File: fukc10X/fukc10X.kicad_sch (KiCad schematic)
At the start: 18 parts, among them J1 SM04B-SRSS-TB, U1 XC6206P332MR, U2 STM32F072CBT6

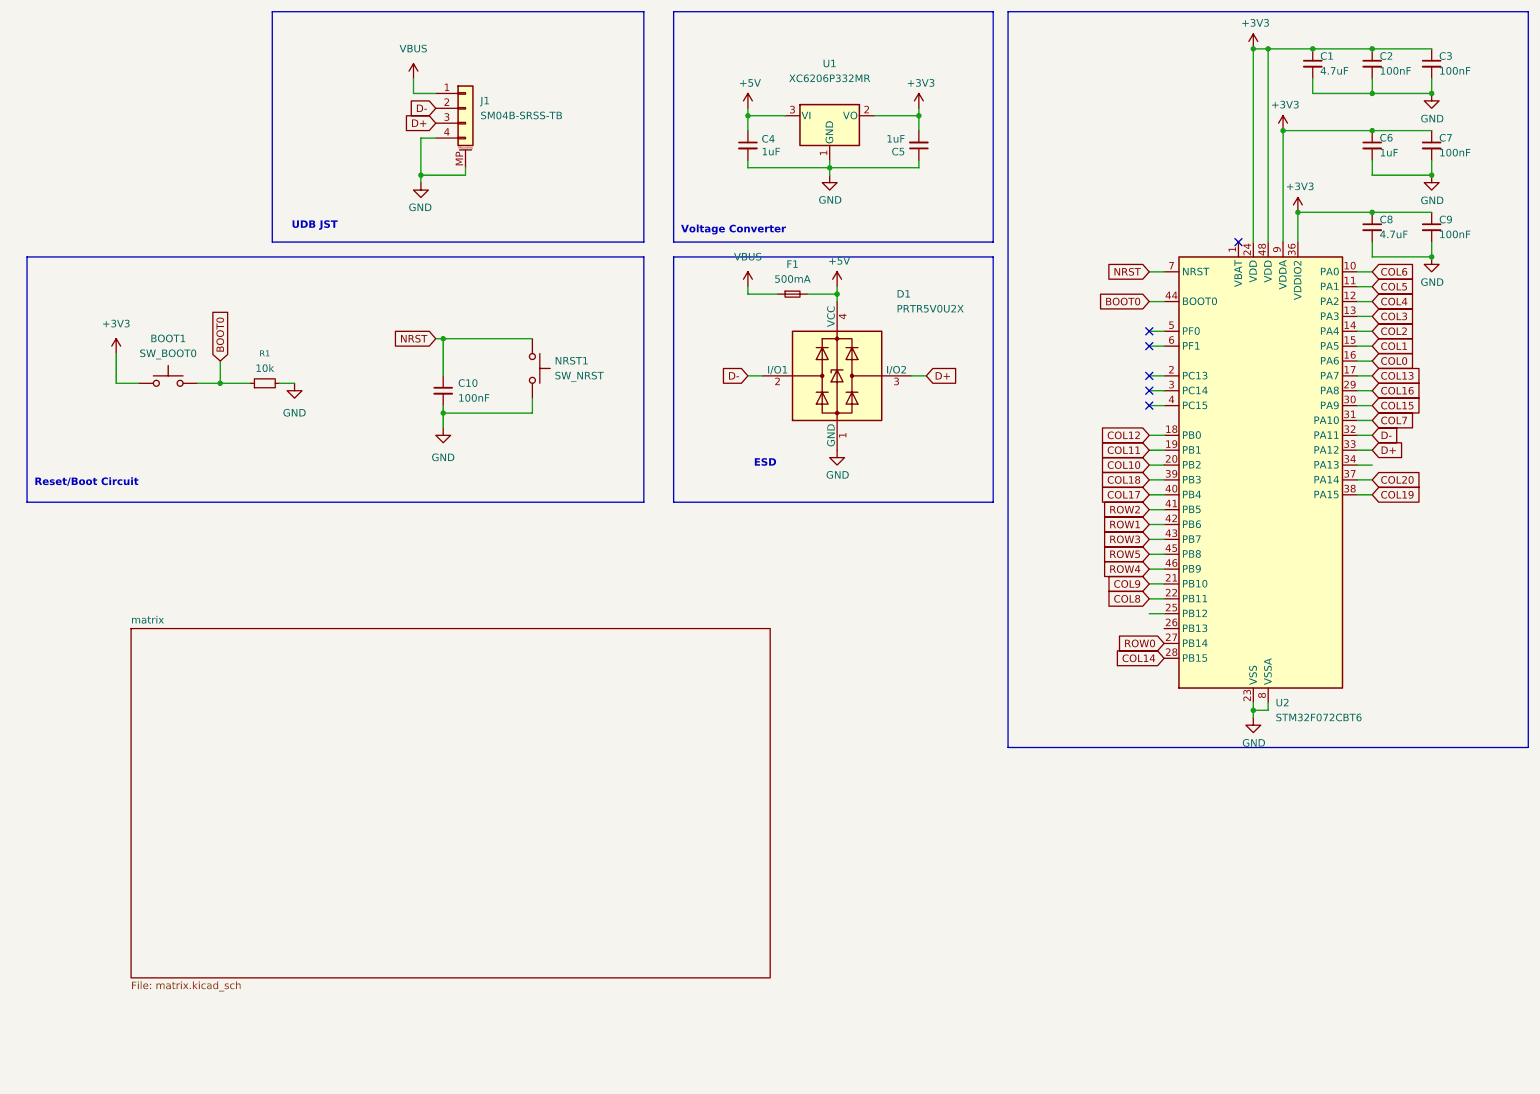
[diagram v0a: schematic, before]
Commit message: Extended Matrix. Added split r-shift and split l-shift. LED support. Removed three of the 4 top right keys because ugly and to make space for indicator leds there
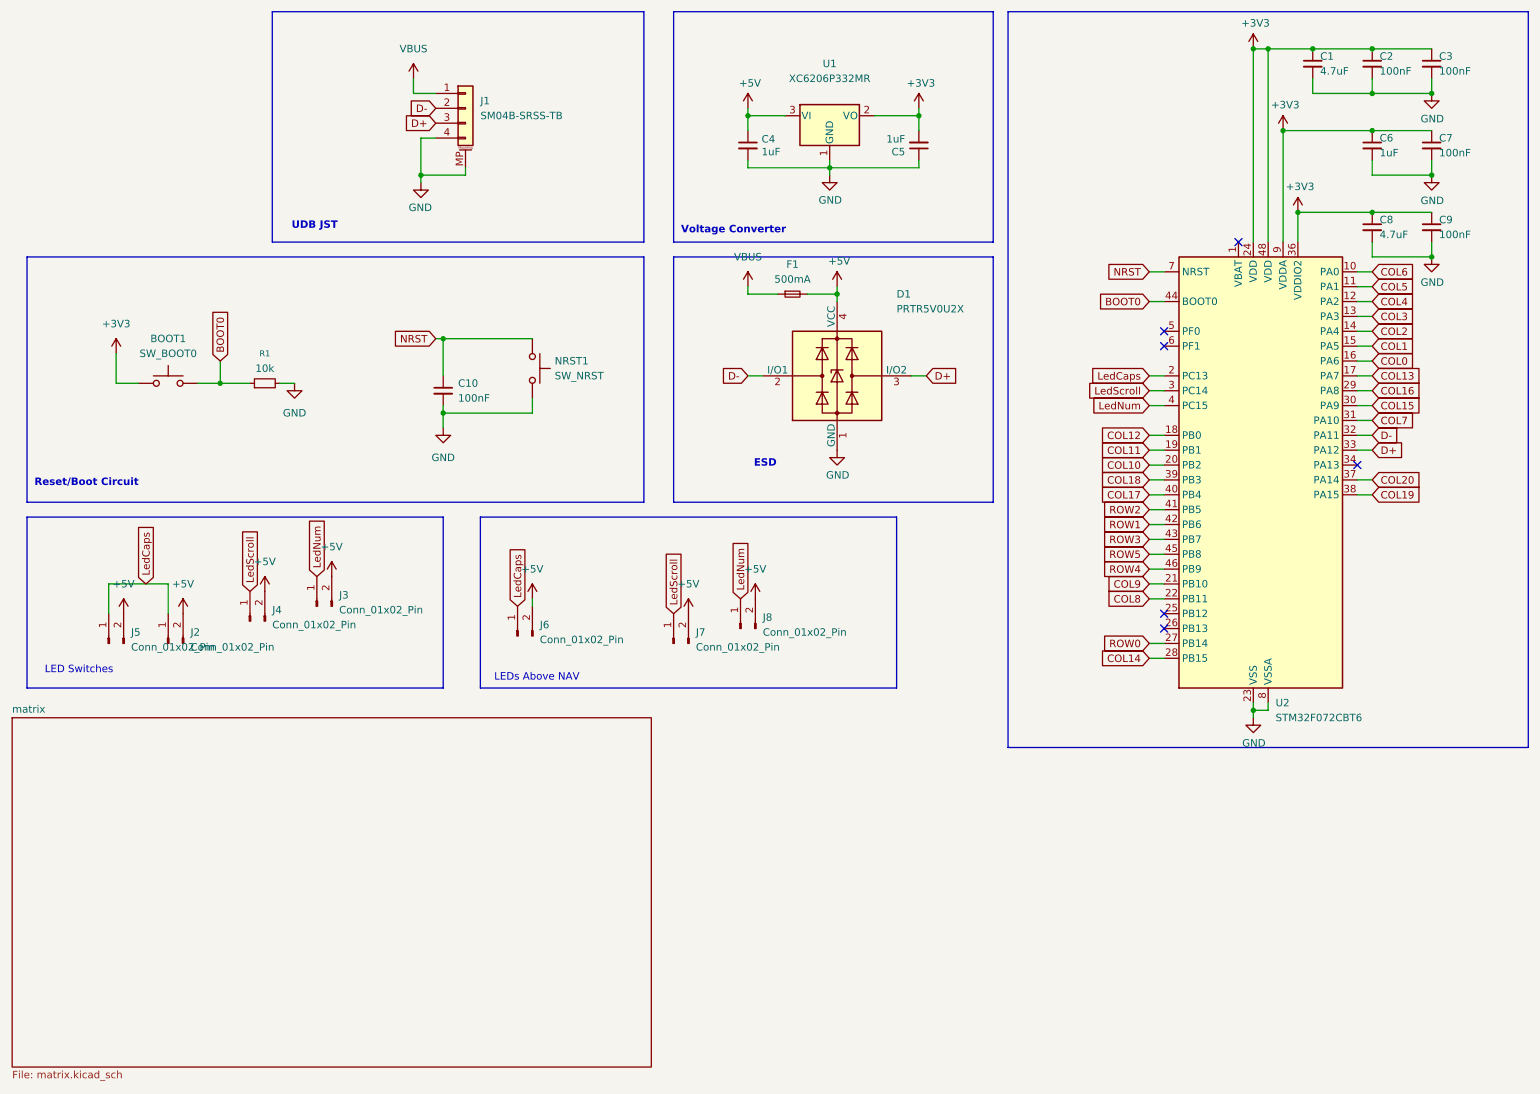
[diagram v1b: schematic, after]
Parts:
- added J2, J3, J4, J6, J7, J8: Conn_01x02_Pin, PCM_marbastlib-mx:LED_MX_3mm, symbol Connector:Conn_01x02_Pin
- added J5: Conn_01x02_Pin, PCM_marbastlib-mx:LED_MX_3mm-ROT, symbol Connector:Conn_01x02_Pin
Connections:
- net +5V: now also J2.2 (Pin_2), J3.2 (Pin_2), J4.2 (Pin_2), J5.2 (Pin_2), J6.2 (Pin_2), J7.2 (Pin_2), J8.2 (Pin_2)
- net LedCaps: now reaches U2.2 (PC13)
- net LedCaps: now also J2.1 (Pin_1), J5.1 (Pin_1), J6.1 (Pin_1)
- net LedScroll: now reaches U2.3 (PC14)
- net LedScroll: now also J4.1 (Pin_1), J7.1 (Pin_1)
- net LedNum: now reaches U2.4 (PC15)
- net LedNum: now also J3.1 (Pin_1), J8.1 (Pin_1)
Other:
- note added: "LED Switches"
- note added: "LEDs Above NAV"

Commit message: Added some Silkscreen Text aswell as spare diodes
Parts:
- added D116, D117, D118, D119, D120, D121, D122, D18, D19, D20, D63, D66: D_Small, Diode_SMD:D_SOD-123, symbol Device:D_Small
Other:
- note added: "Spare Diodes"

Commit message: added split backspace + some updates to the matrix
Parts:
- BOOT1, NRST1: LCSC (none) -> C318884
- C10: LCSC (none) -> C1525
- C2, C3, C7, C9: LCSC C1525 -> C1525
- D116, D117, D118, D119, D120, D121, D122, D18, D19, D20, D63, D66: LCSC (none) -> C81598
- F1: LCSC (none) -> C69688
- R1: LCSC (none) -> C25744
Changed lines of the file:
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@@
 			)
 		)
-		(property "LCSC" "C1525"
+		(property "LCSC" "C1525 "
 			(at 267.97 27.94 0)
 			(hide yes)
@@
 			)
 		)
+		(property "LCSC" "C318884 "
+			(at 50.8 78.74 0)
+			(hide yes)
+			(show_name no)
+			(do_not_autoplace no)
+			(effects
+				(font
+					(size 1.27 1.27)
+				)
+			)
+		)
 		(pin "2"
 		)
@@
 			)
 		)
-		(property "LCSC" "C1525"
+		(property "LCSC" "C1525 "
 			(at 267.97 55.88 0)
 			(hide yes)
@@
 			)
 		)
+		(property "LCSC" "C81598 "
+			(at 168.91 149.86 0)
+			(hide yes)
+			(show_name no)
+			(do_not_autoplace no)
+			(effects
+				(font
+					(size 1.27 1.27)
+				)
+			)
+		)
 		(pin "1"
 		)
@@
 			)
 		)
+		(property "LCSC" "C81598 "
+			(at 181.61 158.75 0)
+			(hide yes)
+			(show_name no)
+			(do_not_autoplace no)
+			(effects
+				(font
+					(size 1.27 1.27)
+				)
+			)
+		)
 		(pin "1"
 		)
@@
 			)
 		)
+		(property "LCSC" "C81598 "
+			(at 168.91 158.75 0)
+			(hide yes)
+			(show_name no)
+			(do_not_autoplace no)
+			(effects
+				(font
+					(size 1.27 1.27)
+				)
+			)
+		)
 		(pin "1"
 		)
@@
 			)
 		)
+		(property "LCSC" "C81598 "
+			(at 176.53 143.51 0)
+			(hide yes)
+			(show_name no)
+			(do_not_autoplace no)
+			(effects
+				(font
+					(size 1.27 1.27)
+				)
+			)
+		)
 		(pin "1"
 		)
@@
 			)
 		)
+		(property "LCSC" "C81598 "
+			(at 162.56 149.86 0)
+			(hide yes)
+			(show_name no)
+			(do_not_autoplace no)
+			(effects
+				(font
+					(size 1.27 1.27)
+				)
+			)
+		)
 		(pin "1"
 		)
@@
 			)
 		)
-		(property "LCSC" "C1525"
+		(property "LCSC" "C1525 "
 			(at 267.97 41.91 0)
 			(hide yes)
@@
 			)
 		)
+		(property "LCSC" "C25744 "
+			(at 67.31 78.74 90)
+			(hide yes)
+			(show_name no)
+			(do_not_autoplace no)
+			(effects
+				(font
+					(size 1.27 1.27)
+				)
+			)
+		)
 		(pin "1"
 		)
@@
 			)
 		)
+		(property "LCSC" "C81598 "
+			(at 181.61 149.86 0)
+			(hide yes)
+			(show_name no)
+			(do_not_autoplace no)
+			(effects
+				(font
+					(size 1.27 1.27)
+				)
+			)
+		)
 		(pin "1"
 		)
@@
 			)
 		)
+		(property "LCSC" "C69688 "
+			(at 157.48 63.5 0)
+			(hide yes)
+			(show_name no)
+			(do_not_autoplace no)
+			(effects
+				(font
+					(size 1.27 1.27)
+				)
+			)
+		)
 		(pin "2"
 		)
@@
 			)
 		)
+		(property "LCSC" "C81598 "
+			(at 162.56 143.51 0)
+			(hide yes)
+			(show_name no)
+			(do_not_autoplace no)
+			(effects
+				(font
+					(size 1.27 1.27)
+				)
+			)
+		)
 		(pin "1"
 		)
@@
 			)
 		)
+		(property "LCSC" "C81598 "
+			(at 161.29 158.75 0)
+			(hide yes)
+			(show_name no)
+			(do_not_autoplace no)
+			(effects
+				(font
+					(size 1.27 1.27)
+				)
+			)
+		)
 		(pin "1"
 		)
@@
 			)
 		)
+		(property "LCSC" "C1525 "
+			(at 97.79 80.01 0)
+			(hide yes)
+			(show_name no)
+			(do_not_autoplace no)
+			(effects
+				(font
+					(size 1.27 1.27)
+				)
+			)
+		)
 		(pin "2"
 		)
@@
 			)
 		)
-		(property "LCSC" "C1525"
+		(property "LCSC" "C1525 "
 			(at 257.81 27.94 0)
 			(hide yes)
@@
 			)
 		)
+		(property "LCSC" "C81598 "
+			(at 170.18 143.51 0)
+			(hide yes)
+			(show_name no)
+			(do_not_autoplace no)
+			(effects
+				(font
+					(size 1.27 1.27)
+				)
+			)
+		)
 		(pin "1"
 		)
@@
 			)
 		)
+		(property "LCSC" "C81598 "
+			(at 175.26 149.86 0)
+			(hide yes)
+			(show_name no)
+			(do_not_autoplace no)
+			(effects
+				(font
+					(size 1.27 1.27)
+				)
+			)
+		)
 		(pin "1"
 		)
@@
 			)
 		)
+		(property "LCSC" "C318884 "
+			(at 113.03 76.2 90)
+			(hide yes)
+			(show_name no)
+			(do_not_autoplace no)
+			(effects
+				(font
+					(size 1.27 1.27)
+				)
+			)
+		)
 		(pin "2"
 		)
@@
 			)
 		)
+		(property "LCSC" "C81598 "
+			(at 182.88 143.51 0)
+			(hide yes)
+			(show_name no)
+			(do_not_autoplace no)
+			(effects
+				(font
+					(size 1.27 1.27)
+				)
+			)
+		)
 		(pin "1"
 		)
@@
 			(at 175.26 158.75 0)
 			(hide yes)
+			(show_name no)
+			(do_not_autoplace no)
+			(effects
+				(font
+					(size 1.27 1.27)
+				)
+			)
+		)
+		(property "LCSC" "C81598 "
+			(at 175.26 158.75 0)
+			(hide yes)

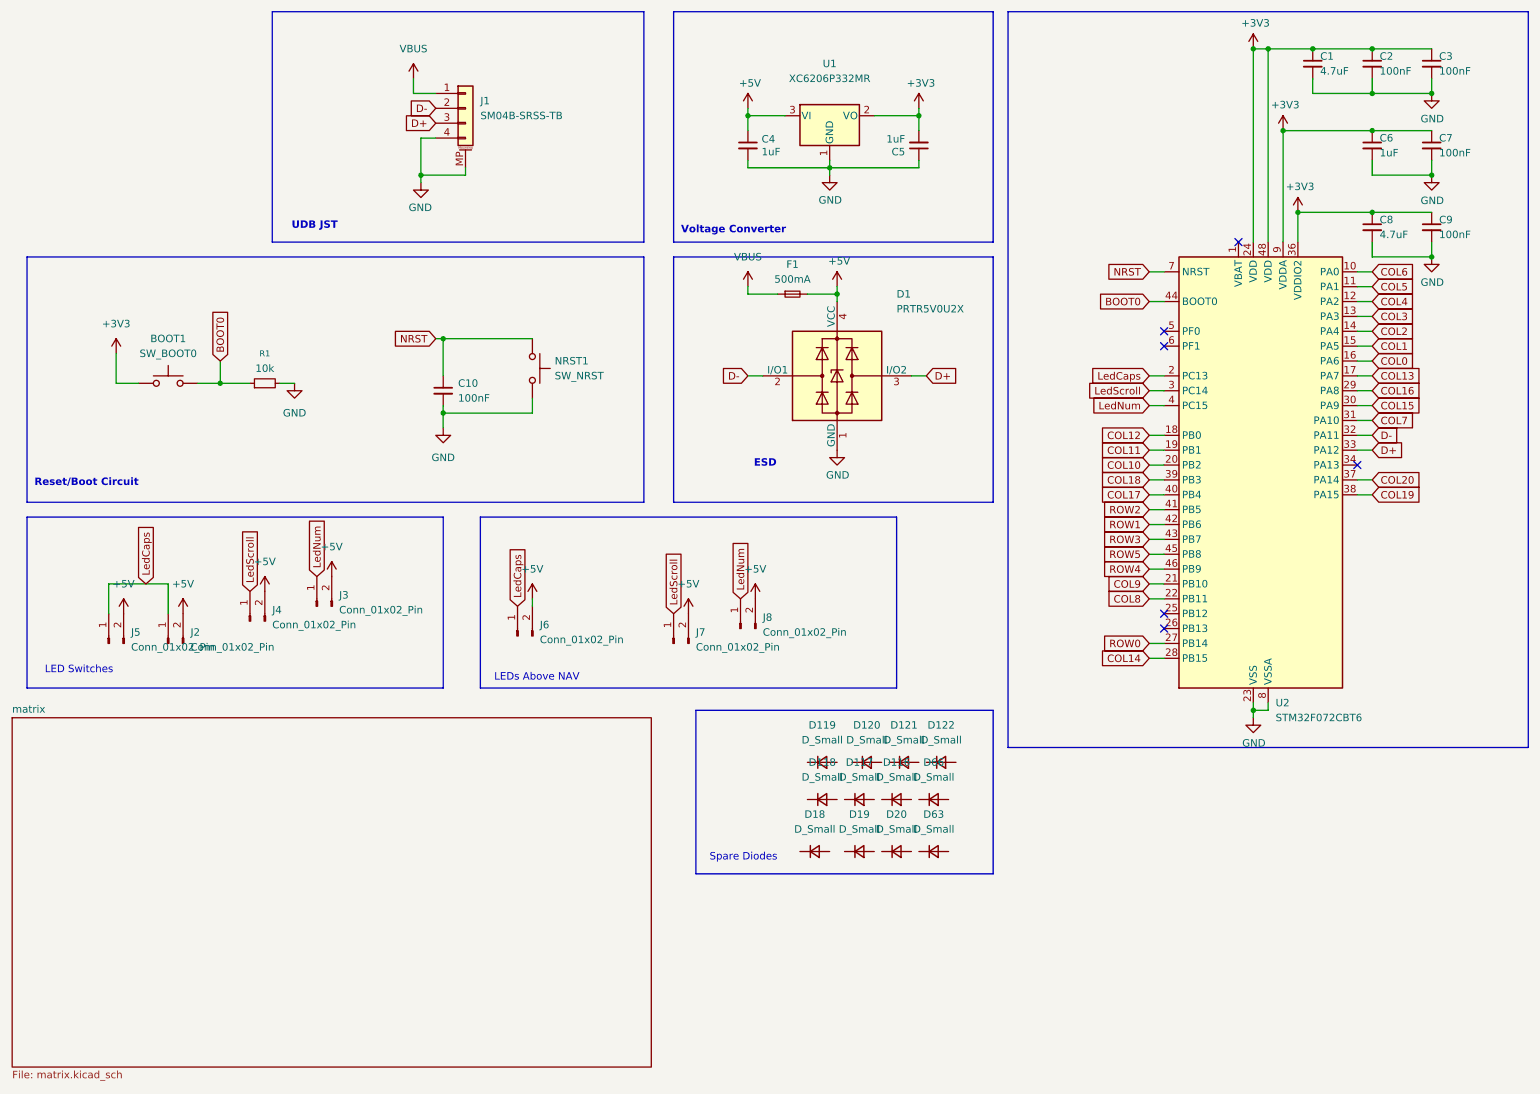
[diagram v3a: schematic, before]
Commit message: updated LED Symbols + removed unnessecarry components for ESD and fusing
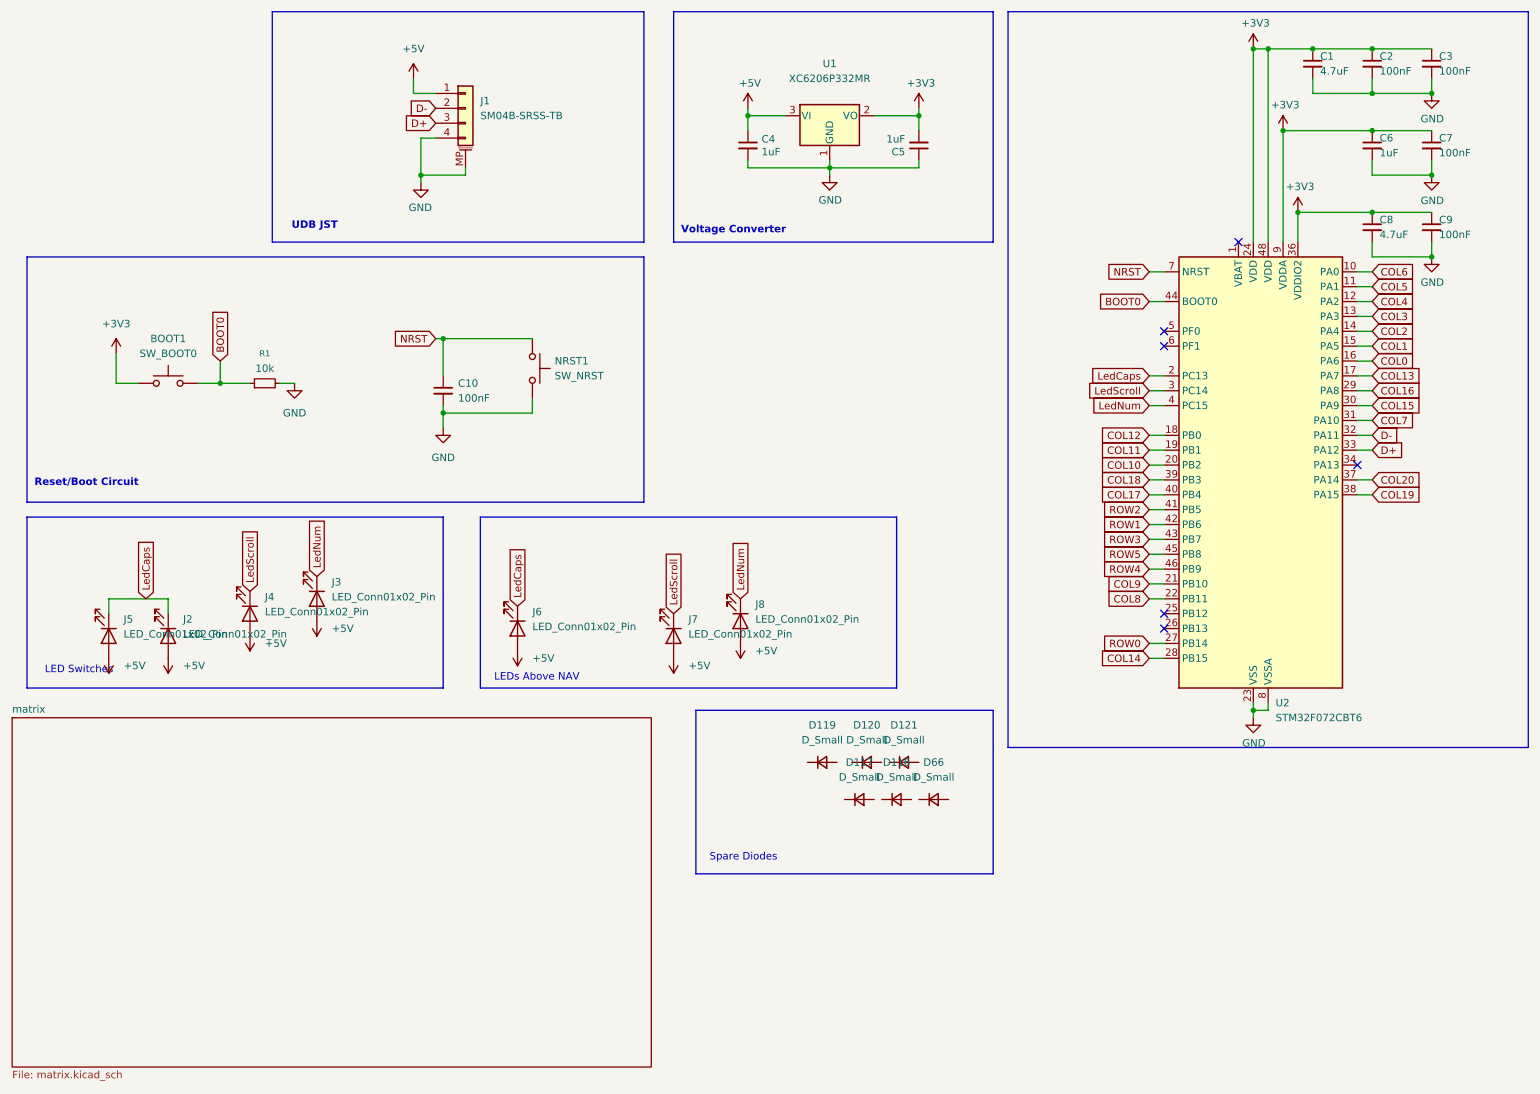
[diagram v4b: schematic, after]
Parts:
- removed D1: PRTR5V0U2X, Package_TO_SOT_SMD:SOT-143, symbol Power_Protection:PRTR5V0U2X
- removed D118, D122, D18, D19, D20, D63: D_Small, Diode_SMD:D_SOD-123, symbol Device:D_Small
- removed F1: 500mA, Fuse:Fuse_1206_3216Metric, symbol Device:Fuse_Small
- J2, J3, J4, J5, J6, J7, J8: value Conn_01x02_Pin -> LED_Conn01x02_Pin; symbol Connector:Conn_01x02_Pin -> Device:LED
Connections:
- net VBUS is gone; now on net +5V: J1.1 (Pin_1)
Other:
- note removed: "ESD"
